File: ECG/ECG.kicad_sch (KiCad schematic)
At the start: 86 parts, among them J1 Conn_01x03, J10 Socket 1x15, J11 Shunt block, J12 Shunt block, J13 Shunt block, J14 Shunt block, J15 Shunt block, J2 Conn_01x03, J3 Conn_01x15, J4 Conn_01x15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

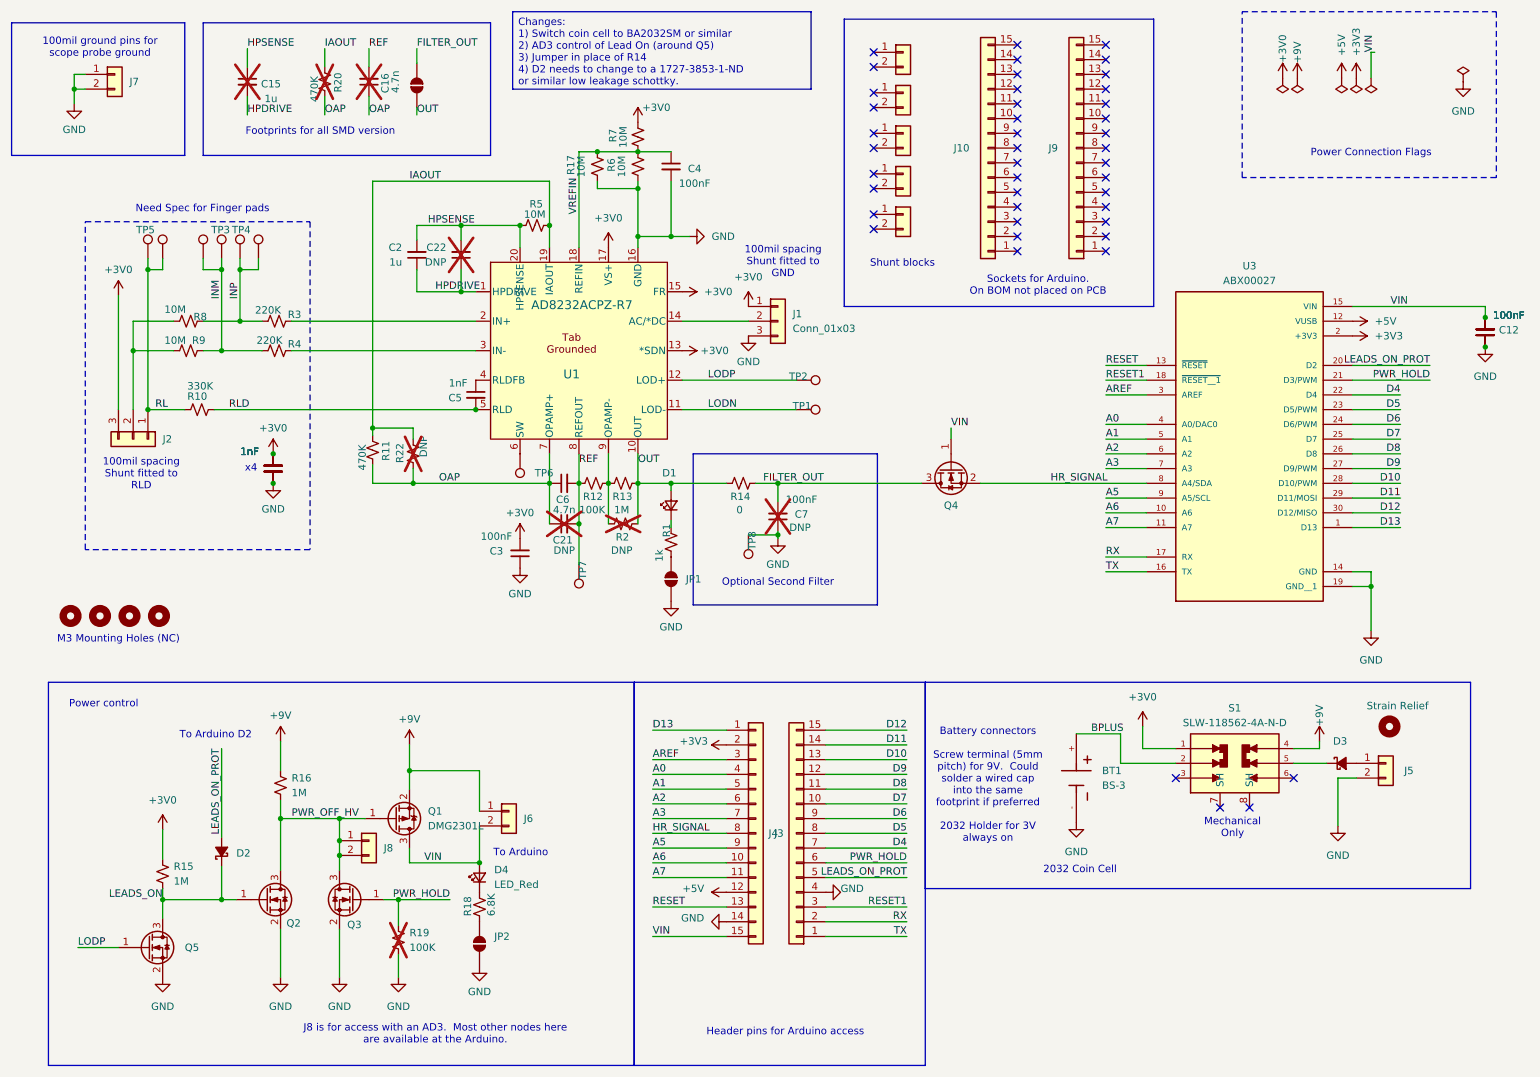
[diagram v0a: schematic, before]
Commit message: Change coin cell holder to one the is dummy "proof"
Close #14
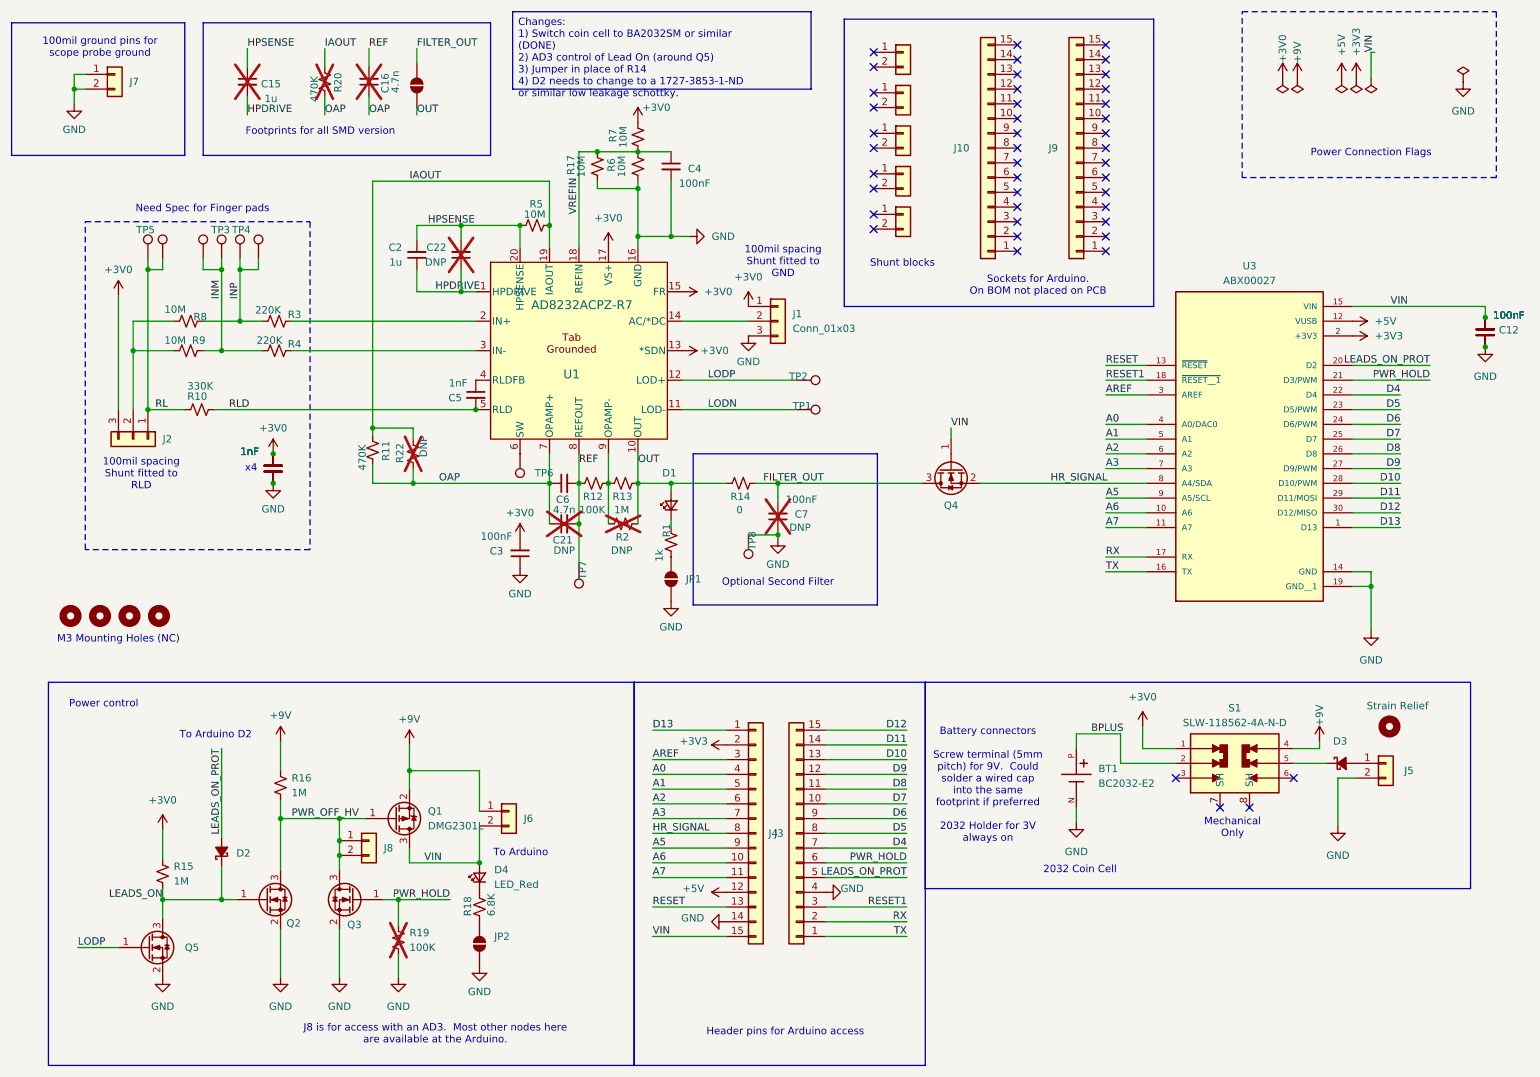
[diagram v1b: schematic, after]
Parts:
- removed BT1: BS-3, ECG_Footprints:BAT_BS-3, symbol EGC_Symbols:BS-3
- added BT1: BC2032-E2, ECG_Footprints:MPD_BC2032-E2, symbol EGC_Symbols:BC2032-E2
- D1, D4: DigiKey PN 732-4978-2-ND -> (none)
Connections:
- net BPLUS: now also BT1.P
- net GND: now also BT1.N
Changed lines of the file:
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@@
 		)
 	)
-	(text_box "Changes:\n1) Switch coin cell to BA2032SM or similar\n2) AD3 control of Lead On (around Q5)\n3) Jumper in place of R14\n4) D2 needs to change to a 1727-3853-1-ND or similar low leakage schottky."
+	(text_box "Changes:\n1) Switch coin cell to BA2032SM or similar (DONE)\n2) AD3 control of Lead On (around Q5)\n3) Jumper in place of R14\n4) D2 needs to change to a 1727-3853-1-ND or similar low leakage schottky."
 		(exclude_from_sim no)
 		(at 102.235 13.97 0)
@@
 	(wire
 		(pts
+			(xy 199.39 138.43) (xy 199.39 140.97)
+		)
+		(stroke
+			(width 0)
+			(type default)
+		)
+	)
+	(wire
+		(pts
 			(xy 52.07 56.515) (xy 52.07 58.42)
 		)
@@
 	(wire
 		(pts
+			(xy 199.39 151.13) (xy 199.39 153.67)
+		)
+		(stroke
+			(width 0)
+			(type default)
+		)
+	)
+	(wire
+		(pts
 			(xy 85.725 30.48) (xy 85.725 31.75)
 		)
@@
 	)
 	(symbol
+		(lib_id "EGC_Symbols:BC2032-E2")
+		(at 199.39 146.05 90)
+		(unit 1)
+		(exclude_from_sim no)
+		(in_bom yes)
+		(on_board yes)
+		(dnp no)
+		(fields_autoplaced yes)
+		(property "Reference" "BT1"
+			(at 203.2 144.437 90)
+			(effects
+				(font
+					(size 1.27 1.27)
+				)
+				(justify right)
+			)
+		)
+		(property "Value" "BC2032-E2"
+			(at 203.2 146.977 90)
+			(effects
+				(font
+					(size 1.27 1.27)
+				)
+				(justify right)
+			)
+		)
+		(property "Footprint" "ECG_Footprints:MPD_BC2032-E2"
+			(at 199.39 146.05 0)
+			(effects
+				(font
+					(size 1.27 1.27)
+				)
+				(justify bottom)
+				(hide yes)
+			)
+		)
+		(property "Datasheet" ""
+			(at 199.39 146.05 0)
+			(effects
+				(font
+					(size 1.27 1.27)
+				)
+				(hide yes)
+			)
+		)
+		(property "Description" ""
+			(at 199.39 146.05 0)
+			(effects
+				(font
+					(size 1.27 1.27)
+				)
+				(hide yes)
+			)
+		)
+		(property "PARTREV" "D"
+			(at 199.39 146.05 0)
+			(effects
+				(font
+					(size 1.27 1.27)
+				)
+				(justify bottom)
+				(hide yes)
+			)
+		)
+		(property "STANDARD" "Manufacturer Recommendation"
+			(at 199.39 146.05 0)
+			(effects
+				(font
+					(size 1.27 1.27)
+				)
+				(justify bottom)
+				(hide yes)
+			)
+		)
+		(property "MANUFACTURER" "MPD"
+			(at 199.39 146.05 0)
+			(effects
+				(font
+					(size 1.27 1.27)
+				)
+				(justify bottom)
+				(hide yes)
+			)
+		)
+		(property "DigikeyPN" "BC2032-E2-ND"
+			(at 199.39 146.05 90)
+			(effects
+				(font
+					(size 1.27 1.27)
+				)
+				(hide yes)
+			)
+		)
+		(pin "N"
+		)
+		(pin "P"
+		)
+		(instances
+			(project ""
+				(path "/e3a79443-8349-4546-8b4f-331bcc551083"
+					(reference "BT1")
+					(unit 1)
+				)
+			)
+		)
+	)
+	(symbol
 		(lib_id "power:+3V0")
 		(at 142.875 64.77 0)
@@
 	)
 	(symbol
-		(lib_id "EGC_Symbols:BS-3")
-		(at 199.39 146.05 270)
-		(unit 1)
-		(exclude_from_sim no)
-		(in_bom yes)
-		(on_board yes)
-		(dnp no)
-		(fields_autoplaced yes)
-		(property "Reference" "BT1"
-			(at 203.835 144.7799 90)
-			(effects
-				(font
-					(size 1.27 1.27)
-				)
-				(justify left)
-			)
-		)
-		(property "Value" "BS-3"
-			(at 203.835 147.3199 90)
-			(effects
-				(font
-					(size 1.27 1.27)
-				)
-				(justify left)
-			)
-		)
-		(property "Footprint" "ECG_Footprints:BAT_BS-3"
-			(at 199.39 146.05 0)
-			(effects
-				(font
-					(size 1.27 1.27)
-				)
-				(justify bottom)
-				(hide yes)
-			)
-		)
-		(property "Datasheet" ""
-			(at 199.39 146.05 0)
-			(effects
-				(font
-					(size 1.27 1.27)
-				)
-				(hide yes)
-			)
-		)
-		(property "Description" ""
-			(at 199.39 146.05 0)
-			(effects
-				(font
-					(size 1.27 1.27)
-				)
-				(hide yes)
-			)
-		)
-		(property "PARTREV" "F"
-			(at 199.39 146.05 0)
-			(effects
-				(font
-					(size 1.27 1.27)
-				)
-				(justify bottom)
-				(hide yes)
-			)
-		)
-		(property "STANDARD" "Manufacturer recommendations"
-			(at 199.39 146.05 0)
-			(effects
-				(font
-					(size 1.27 1.27)
-				)
-				(justify bottom)
-				(hide yes)
-			)
-		)
-		(property "MAXIMUM_PACKAGE_HEIGHT" "6.75mm"
-			(at 199.39 146.05 0)
-			(effects
-				(font
-					(size 1.27 1.27)
-				)
-				(justify bottom)
-				(hide yes)
-			)
-		)
-		(property "MANUFACTURER" "MPD"
-			(at 199.39 146.05 0)
-			(effects
-				(font
-					(size 1.27 1.27)
-				)
-				(justify bottom)
-				(hide yes)
-			)
-		)
-		(property "DigikeyPN" "BS-3-ND"
-			(at 199.39 146.05 90)
-			(effects
-				(font
-					(size 1.27 1.27)
-				)
-				(hide yes)
-			)
-		)
-		(property "Sim.Device" ""
-			(at 199.39 146.05 90)
-			(effects
-				(font
-					(size 1.27 1.27)
-				)
-				(hide yes)
-			)
-		)
-		(property "Sim.Pins" ""
-			(at 199.39 146.05 90)
-			(effects
-				(font
-					(size 1.27 1.27)
-				)
-				(hide yes)
-			)
-		)
-		(pin "+"
-		)
-		(pin "-"
-		)
-		(instances
-			(project ""
-				(path "/e3a79443-8349-4546-8b4f-331bcc551083"
-					(reference "BT1")
-					(unit 1)
-				)
-			)
-		)
-	)
-	(symbol
 		(lib_id "power:GND")
 		(at 41.91 180.34 0)
@@
 			)
 		)
-		(property "DigiKey PN" "732-4978-2-ND"
-			(at 96.52 163.195 0)
-			(effects
-				(font
-					(size 1.27 1.27)
-				)
-				(hide yes)
-			)
-		)
 		(property "BIN" "1000"
 			(at 96.52 163.195 0)
@@
 			(at 129.54 99.06 0)
 			(effects
-				(font
-					(size 1.27 1.27)
-				)
-				(hide yes)
-			)
-		)
-		(property "DigiKey PN" "732-4978-2-ND"
-			(at 129.54 99.06 0)
-			(effects
